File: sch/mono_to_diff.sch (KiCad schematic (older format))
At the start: 28 parts

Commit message: First commit
 On branch development

	new file:   README.md
	renamed:    sch/mono_to_diff.pro -> mono_to_diff.pro
	new file:   pcb/mono_to_diff.kicad_pcb
	new file:   pcb/mono_to_diff.net
	new file:   pcb/mono_to_diff.pro
	modified:   sch/mono_to_diff-cache.lib
	deleted:    sch/mono_to_diff-rescue.lib
	modified:   sch/mono_to_diff.pro
	modified:   sch/mono_to_diff.sch
	deleted:    sch/reference.lib
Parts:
- added C10, C11, C15, C16: 10nF-50V-10p-Ceramic-0805, RCL_SMT:SOLEIL-0805, symbol 10nF-50V-10p-Ceramic-0805
- added C13, C14, C4, C7: 100nF-50V-10p-Ceramic-0805, RCL_SMT:SOLEIL-0805, symbol 100nF-50V-10p-Ceramic-0805
- added C2, C5: 10uF-16V-20p-Al-TypeB, RCL_SMT:SOLEIL-TYPEB, symbol 10uF-16V-20p-Al-TypeB
- added FIX1, FIX2, FIX3, FIX4: D_2mm8, holes:SOLEIL-D_2mm8, symbol D_2mm8
- added R13: 1K87-0.125W-1P-0805, RCL_SMT:SOLEIL-0805, symbol 1K87-0.125W-1P-0805
- added R14: 1K-0.125W-1P-0805, RCL_SMT:SOLEIL-0805, symbol 1K-0.125W-1P-0805
- added R15, R16: 1K58-0.125W-1P-0805, RCL_SMT:SOLEIL-0805, symbol 1K58-0.125W-1P-0805
- added R17, R18: 0R-0.125W-1P-0805, RCL_SMT:SOLEIL-0805, symbol 0R-0.125W-1P-0805
- added U3: LT6600CS8-2.5, SO:SOLEIL-SOIC8NB, symbol LT6600CS8-2.5
- C1, C12, C6, C8, C9: renamed from C?; footprint SOLEIL-0805 -> RCL_SMT:SOLEIL-0805
- C3: renamed from C?; footprint SOLEIL-PC-B -> RCL_SMT:SOLEIL-PC-B
- J1, J3, J5: renamed from J?; footprint SOLEIL-24_243 -> PSU_connectors:SOLEIL-24_243
- J2, J4, J6, J7: renamed from J?; footprint SOLEIL-SMA-132134 -> SMA_connectors:SOLEIL-SMA-132134
- R1, R10, R11, R12, R2, R3, R4, R5, R6, R7, R8, R9: renamed from R?; footprint SOLEIL-0805 -> RCL_SMT:SOLEIL-0805
- U1: renamed from U?; footprint SOLEIL-SOT23-6 -> SOT23:SOLEIL-SOT23-6
- U2: renamed from U?; footprint SOLEIL-SOIC8NB -> SO:SOLEIL-SOIC8NB
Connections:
- net GND: now also C10.2, C11.2, C13.2, C14.2, C15.2, C16.2, C2.2, C4.2, C5.1, C7.2, FIX1.1, FIX2.1, FIX3.1, FIX4.1, R14.2, R16.1
- net VCC: now also J1.1, J1.2, C10.1, C15.1, C2.1, C4.1, R13.1, U3.3 (V+)
- net VDD: now also J3.1, J3.2, C11.1, C16.1, C5.2, C7.1, U3.6 (V-)
- net at R4.1, R6.2, U2.5 (+): now also R15.1
- net OUT_P: now reaches C12.1, J6.1 (P), R11.1
- net OUT_P: now also R17.2
- net OUT_N: now reaches C12.2, J7.1 (P), R12.1
- net OUT_N: now also R18.2
- new net: R15.2, U3.1 (-)
- new net: C13.1, R13.2, R14.1, U3.2
- new net: R17.1, U3.4
- new net: R18.1, U3.5
- new net: C14.1, U3.7
- new net: R16.2, U3.8 (+)
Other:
- moved on the sheet: C1, C12, C3, C6, C8, C9, J1, J2, J3, J4, J5, J6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

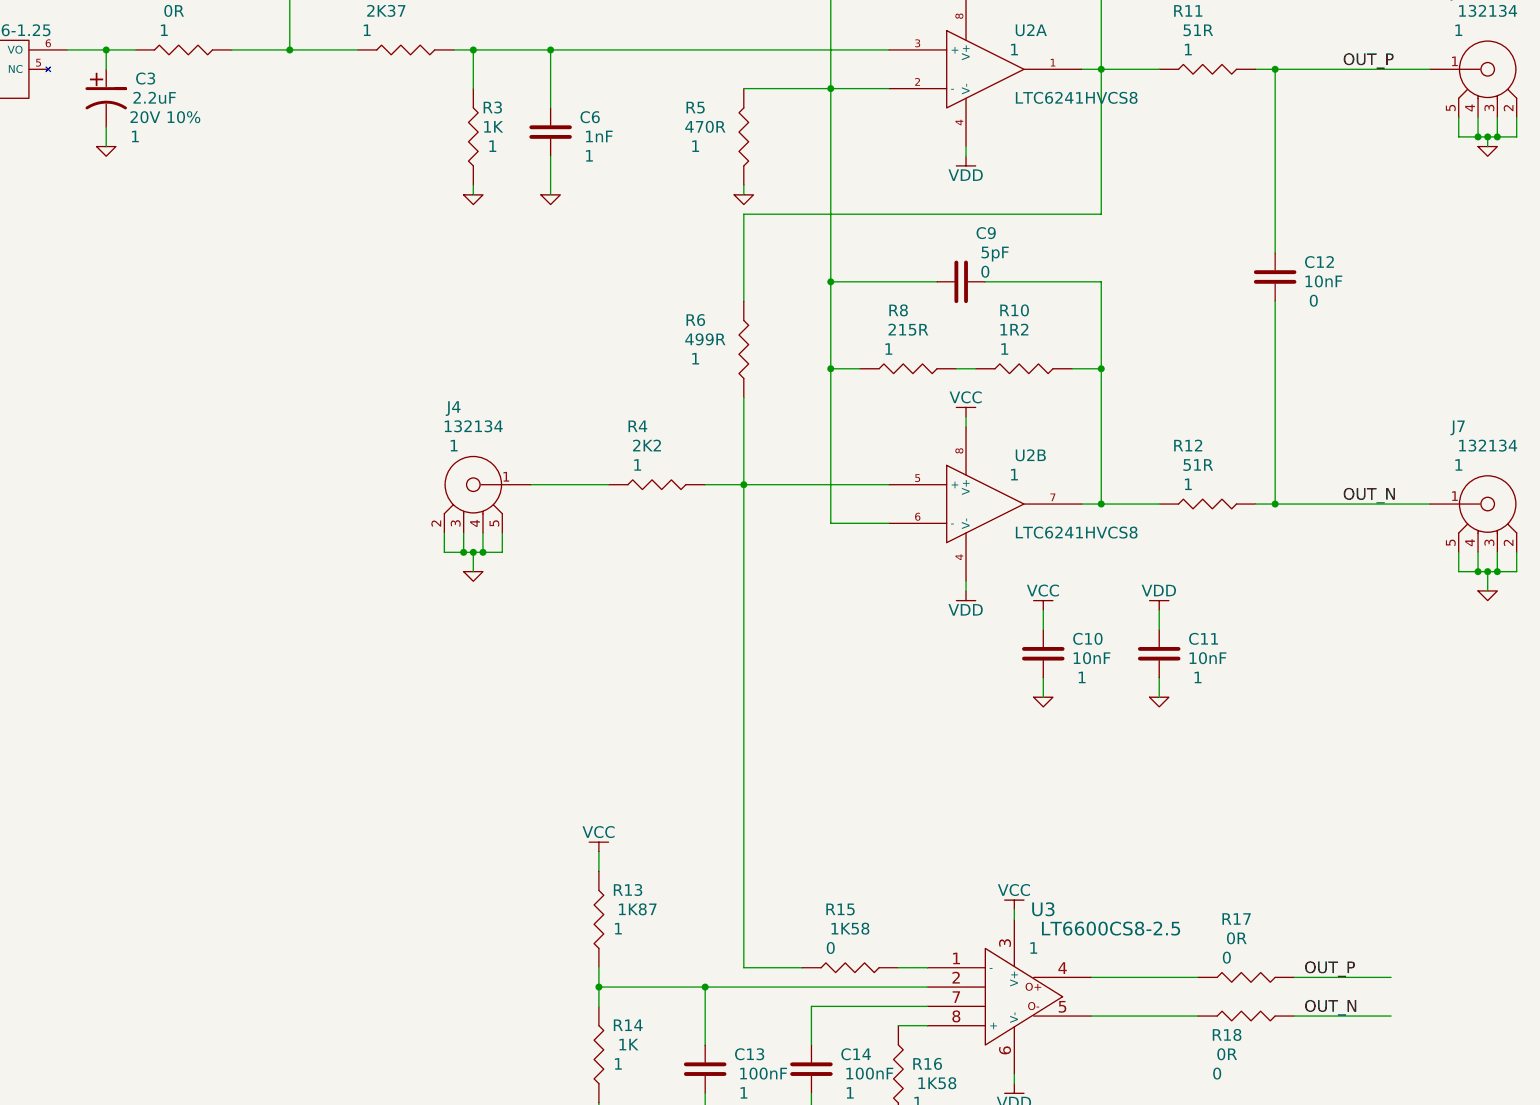
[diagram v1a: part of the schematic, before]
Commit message: Added a low pass filter
 On branch development

	modified:   pcb/mono_to_diff.kicad_pcb
	modified:   pcb/mono_to_diff.net
	modified:   sch/mono_to_diff-cache.lib
	modified:   sch/mono_to_diff.pro
	modified:   sch/mono_to_diff.sch
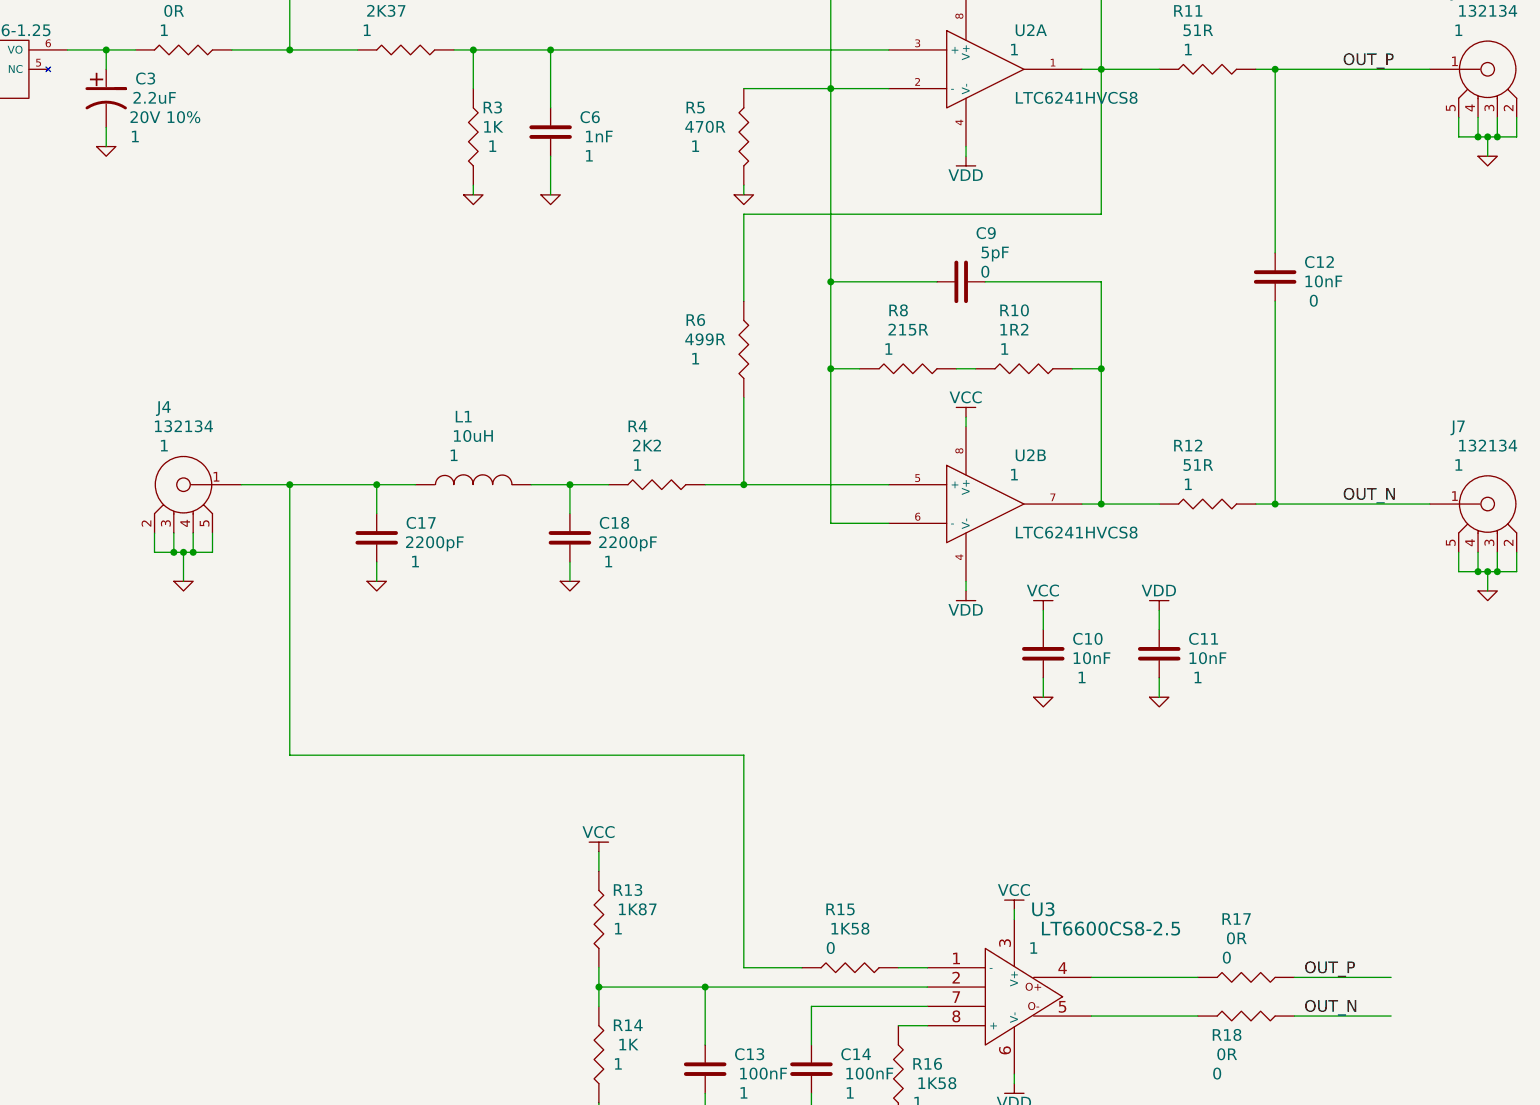
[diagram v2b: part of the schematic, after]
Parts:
- added C17, C18: 2200pF-50V-5p-Ceramic-0805, RCL_SMT:SOLEIL-0805, symbol 2200pF-50V-5p-Ceramic-0805
- added L1: 10uH-140mA-5p-36MHz-1210, RCL_SMT:SOLEIL-1210, symbol 10uH-140mA-5p-36MHz-1210
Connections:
- net GND: now also C17.2, C18.2
- net at R4.1, R6.2, U2.5 (+): no longer R15.1
- net at R4.2: now also C18.1, L1.2; no longer J4.1 (P)
- new net: C17.1, J4.1 (P), L1.1, R15.1
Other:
- moved on the sheet: J4
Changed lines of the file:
@@
 LIBS:CPCI_connectors
 LIBS:resistors_0805
+LIBS:inductors_1210
 LIBS:mono_to_diff-cache
 EELAYER 25 0
@@
 Wire Wire Line
 	7650 4500 8600 4500
-Wire Wire Line
-	7850 4050 7850 7000
 $Comp
 L 51R-0.125W-1P-0805 R11
@@
 L 132134 J4
 U 1 1 557B1D39
-P 6750 4500
-F 0 "J4" H 7150 4900 60  0000 C CNN
-F 1 "132134" H 7050 4800 60  0000 C CNN
-F 2 "SMA_connectors:SOLEIL-SMA-132134" H 7700 4650 60  0001 C CNN
-F 3 "" H 6750 4500 60  0000 C CNN
-F 4 "Amphenol Connex" H 7600 4550 60  0001 C CNN "Manufacturer"
-F 5 "132134" H 7400 4450 60  0001 C CNN "Manufacturer ref"
-F 6 "Farnell" H 7400 4350 60  0001 C CNN "Supplier"
-F 7 "2112465" H 7450 4250 60  0001 C CNN "Supplier ref"
-F 8 "1" H 7150 4700 60  0000 C CNN "Qty"
-F 9 "-" H 7350 4150 60  0001 C CNN "Desc1"
-F 10 "-" H 7350 4050 60  0001 C CNN "Desc2"
-F 11 "-" H 7350 3950 60  0001 C CNN "Desc3"
-F 12 "-" H 7450 3950 60  0001 C CNN "Desc4"
-F 13 "SMA 132134" H 7500 3850 60  0001 C CNN "Case"
-F 14 "3.65" H 7350 3750 60  0001 C CNN "Price"
-	1    6750 4500
+P 5250 4500
+F 0 "J4" H 5650 4900 60  0000 C CNN
+F 1 "132134" H 5550 4800 60  0000 C CNN
+F 2 "SMA_connectors:SOLEIL-SMA-132134" H 6200 4650 60  0001 C CNN
+F 3 "" H 5250 4500 60  0000 C CNN
+F 4 "Amphenol Connex" H 6100 4550 60  0001 C CNN "Manufacturer"
+F 5 "132134" H 5900 4450 60  0001 C CNN "Manufacturer ref"
+F 6 "Farnell" H 5900 4350 60  0001 C CNN "Supplier"
+F 7 "2112465" H 5950 4250 60  0001 C CNN "Supplier ref"
+F 8 "1" H 5650 4700 60  0000 C CNN "Qty"
+F 9 "-" H 5850 4150 60  0001 C CNN "Desc1"
+F 10 "-" H 5850 4050 60  0001 C CNN "Desc2"
+F 11 "-" H 5850 3950 60  0001 C CNN "Desc3"
+F 12 "-" H 5950 3950 60  0001 C CNN "Desc4"
+F 13 "SMA 132134" H 6000 3850 60  0001 C CNN "Case"
+F 14 "3.65" H 5850 3750 60  0001 C CNN "Price"
+	1    5250 4500
 	-1   0    0    -1
 $EndComp
@@
 L GND #PWR06
 U 1 1 557B20A9
-P 6450 4950
-F 0 "#PWR06" H 6450 4950 30  0001 C CNN
-F 1 "GND" H 6450 4880 30  0001 C CNN
-F 2 "" H 6450 4950 60  0000 C CNN
-F 3 "" H 6450 4950 60  0000 C CNN
-	1    6450 4950
+P 4950 5000
+F 0 "#PWR06" H 4950 5000 30  0001 C CNN
+F 1 "GND" H 4950 4930 30  0001 C CNN
+F 2 "" H 4950 5000 60  0000 C CNN
+F 3 "" H 4950 5000 60  0000 C CNN
+	1    4950 5000
 	1    0    0    -1
 $EndComp
@@
 L GND #PWR08
 U 1 1 557B2135
-P 11700 2750
-F 0 "#PWR08" H 11700 2750 30  0001 C CNN
-F 1 "GND" H 11700 2680 30  0001 C CNN
-F 2 "" H 11700 2750 60  0000 C CNN
-F 3 "" H 11700 2750 60  0000 C CNN
-	1    11700 2750
+P 11700 2800
+F 0 "#PWR08" H 11700 2800 30  0001 C CNN
+F 1 "GND" H 11700 2730 30  0001 C CNN
+F 2 "" H 11700 2800 60  0000 C CNN
+F 3 "" H 11700 2800 60  0000 C CNN
+	1    11700 2800
 	1    0    0    -1
 $EndComp
@@
 	6750 4500 7150 4500
 Wire Wire Line
-	6600 4850 6600 4750
-Wire Wire Line
-	6300 4850 6600 4850
-Wire Wire Line
-	6300 4850 6300 4750
-Wire Wire Line
-	6450 4950 6450 4850
-Connection ~ 6450 4850
-Wire Wire Line
-	6400 4750 6400 4850
-Connection ~ 6400 4850
-Wire Wire Line
-	6500 4750 6500 4850
-Connection ~ 6500 4850
+	5100 4850 5100 4750
+Wire Wire Line
+	4800 4850 5100 4850
+Wire Wire Line
+	4800 4850 4800 4750
+Wire Wire Line
+	4950 5000 4950 4850
+Connection ~ 4950 4850
+Wire Wire Line
+	4900 4750 4900 4850
+Connection ~ 4900 4850
+Wire Wire Line
+	5000 4750 5000 4850
+Connection ~ 5000 4850
 Connection ~ 10600 4600
 Connection ~ 10600 2350
@@
 	11550 2700 11550 2600
 Wire Wire Line
-	11700 2700 11700 2750
+	11700 2700 11700 2800
 Connection ~ 11700 2700
 Wire Wire Line
@@
 Wire Wire Line
 	10000 8250 10000 8150
+Wire Wire Line
+	7850 4500 7850 4050
+$Comp
+L 2200pF-50V-5p-Ceramic-0805 C17
+U 1 1 55897206
+P 5950 4650
+F 0 "C17" H 6100 4600 60  0000 L CNN
+F 1 "2200pF-50V-5p-Ceramic-0805" H 6100 4200 60  0001 L CNN
+F 2 "RCL_SMT:SOLEIL-0805" H 6600 4100 60  0001 C CNN
+F 3 "" H 5950 4650 60  0000 C CNN
+F 4 "KEMET" H 6250 4000 60  0001 C CNN "Manufacturer"
+F 5 "C0805C222J5GACAUTO" H 6600 3900 60  0001 C CNN "Manufacturer ref"
+F 6 "Farnell" H 6250 3800 60  0001 C CNN "Supplier"
+F 7 "2070464" H 6300 3700 60  0001 C CNN "Supplier ref"
+F 8 "1" H 6150 4400 60  0000 C CNN "Qty"
+F 9 "2200pF" H 6250 4500 60  0000 C CNN "Desc1"
+F 10 "50V" H 6200 4300 60  0001 C CNN "Desc2"
+F 11 "5%" H 6400 4300 60  0001 C CNN "Desc3"
+F 12 "C0G" H 6600 4300 60  0001 C CNN "Desc4"
+F 13 "0805" H 6200 3600 60  0001 C CNN "Case"
+F 14 "0.10" H 6200 3500 60  0001 C CNN "Price"
+	1    5950 4650
+	1    0    0    -1
+$EndComp
+$Comp
+L GND #PWR044
+U 1 1 55897325
+P 5950 5000
+F 0 "#PWR044" H 5950 5000 30  0001 C CNN
+F 1 "GND" H 5950 4930 30  0001 C CNN
+F 2 "" H 5950 5000 60  0000 C CNN
+F 3 "" H 5950 5000 60  0000 C CNN
+	1    5950 5000
+	1    0    0    -1
+$EndComp
+Wire Wire Line
+	5950 4900 5950 5000
+$Comp
+L 2200pF-50V-5p-Ceramic-0805 C18
+U 1 1 558973DC
+P 6950 4650
+F 0 "C18" H 7100 4600 60  0000 L CNN
+F 1 "2200pF-50V-5p-Ceramic-0805" H 7100 4200 60  0001 L CNN
+F 2 "RCL_SMT:SOLEIL-0805" H 7600 4100 60  0001 C CNN
+F 3 "" H 6950 4650 60  0000 C CNN
+F 4 "KEMET" H 7250 4000 60  0001 C CNN "Manufacturer"
+F 5 "C0805C222J5GACAUTO" H 7600 3900 60  0001 C CNN "Manufacturer ref"
+F 6 "Farnell" H 7250 3800 60  0001 C CNN "Supplier"
+F 7 "2070464" H 7300 3700 60  0001 C CNN "Supplier ref"
+F 8 "1" H 7150 4400 60  0000 C CNN "Qty"
+F 9 "2200pF" H 7250 4500 60  0000 C CNN "Desc1"
+F 10 "50V" H 7200 4300 60  0001 C CNN "Desc2"
+F 11 "5%" H 7400 4300 60  0001 C CNN "Desc3"
+F 12 "C0G" H 7600 4300 60  0001 C CNN "Desc4"
+F 13 "0805" H 7200 3600 60  0001 C CNN "Case"
+F 14 "0.10" H 7200 3500 60  0001 C CNN "Price"
+	1    6950 4650
+	1    0    0    -1
+$EndComp
+$Comp
+L GND #PWR045
+U 1 1 558973E2
+P 6950 5000
+F 0 "#PWR045" H 6950 5000 30  0001 C CNN
+F 1 "GND" H 6950 4930 30  0001 C CNN
+F 2 "" H 6950 5000 60  0000 C CNN
+F 3 "" H 6950 5000 60  0000 C CNN
+	1    6950 5000
+	1    0    0    -1
+$EndComp
+Wire Wire Line
+	6950 4900 6950 5000
+Wire Wire Line
+	5250 4500 6150 4500
+Wire Wire Line
+	5950 4650 5950 4500
+Connection ~ 5950 4500
+Wire Wire Line
+	6950 4650 6950 4500
+Connection ~ 6950 4500
+Wire Wire Line
+	7850 7000 7850 5900
+Wire Wire Line
+	7850 5900 5500 5900
+Wire Wire Line
+	5500 5900 5500 4500
+Connection ~ 5500 4500
+$Comp
+L 10uH-140mA-5p-36MHz-1210 L1
+U 1 1 5589B11E
+P 6150 4500
+F 0 "L1" V 6500 4250 60  0000 C CNN
+F 1 "10uH-140mA-5p-36MHz-1210" H 6900 3950 60  0001 C CNN
+F 2 "RCL_SMT:SOLEIL-1210" H 6700 3850 60  0001 C CNN
+F 3 "" H 6150 4500 60  0000 C CNN
+F 4 "Panasonic" H 6450 3750 60  0001 C CNN "Manufacturer"
+F 5 "ELJFA100JF" H 6500 3650 60  0001 C CNN "Manufacturer ref"
+F 6 "Farnell" H 6400 3550 60  0001 C CNN "Supplier"
+F 7 "	1198456" H 6400 3450 60  0001 C CNN "Supplier ref"
+F 8 "1" V 6300 4300 60  0000 C CNN "Qty"
+F 9 "10uH" V 6400 4200 60  0000 C CNN "Desc1"
+F 10 "140mA" H 6700 3300 60  0001 C CNN "Desc2"
+F 11 "5%" H 7000 3300 60  0001 C CNN "Desc3"
+F 12 "36MHz" H 7250 3300 60  0001 C CNN "Desc4"
+F 13 "1210" H 6350 3300 60  0001 C CNN "Case"
+F 14 "0.09" H 6350 3200 60  0001 C CNN "Price"
+	1    6150 4500
+	0    -1   -1   0
+$EndComp
 $EndSCHEMATC
